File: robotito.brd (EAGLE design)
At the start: 76.2 x 76.2 mm, 53 parts, among them IC1 7805T, IC2 L298, IC3 L298, J1 22-27-2031-03, J10 22-27-2031-03, J11 22-27-2031-03, J2 22-27-2031-03, J3 22-27-2031-03, J4 22-27-2031-03, J5 22-27-2031-03, J6 22-27-2031-03, J7 22-27-2031-03, J8 22-27-2031-03, J9 22-27-2031-03

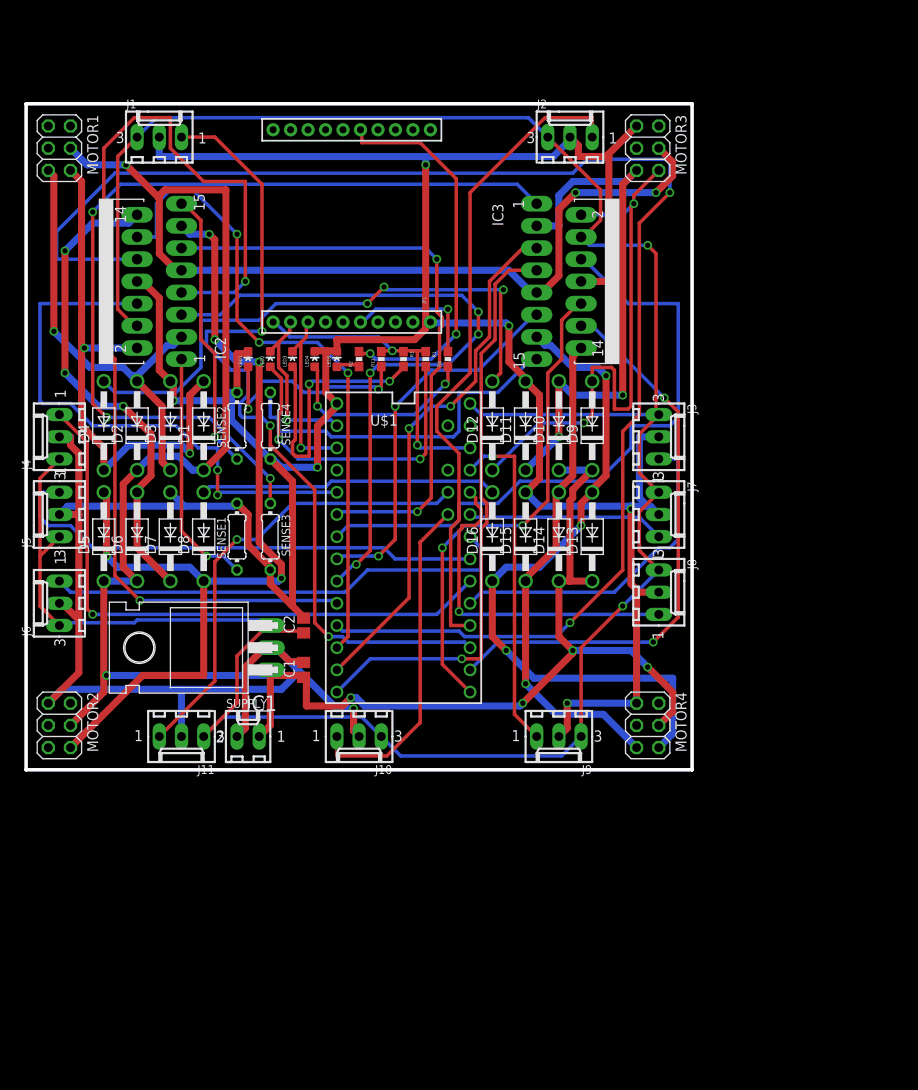
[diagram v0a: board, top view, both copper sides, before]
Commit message: Board is routing good with ~100 vias
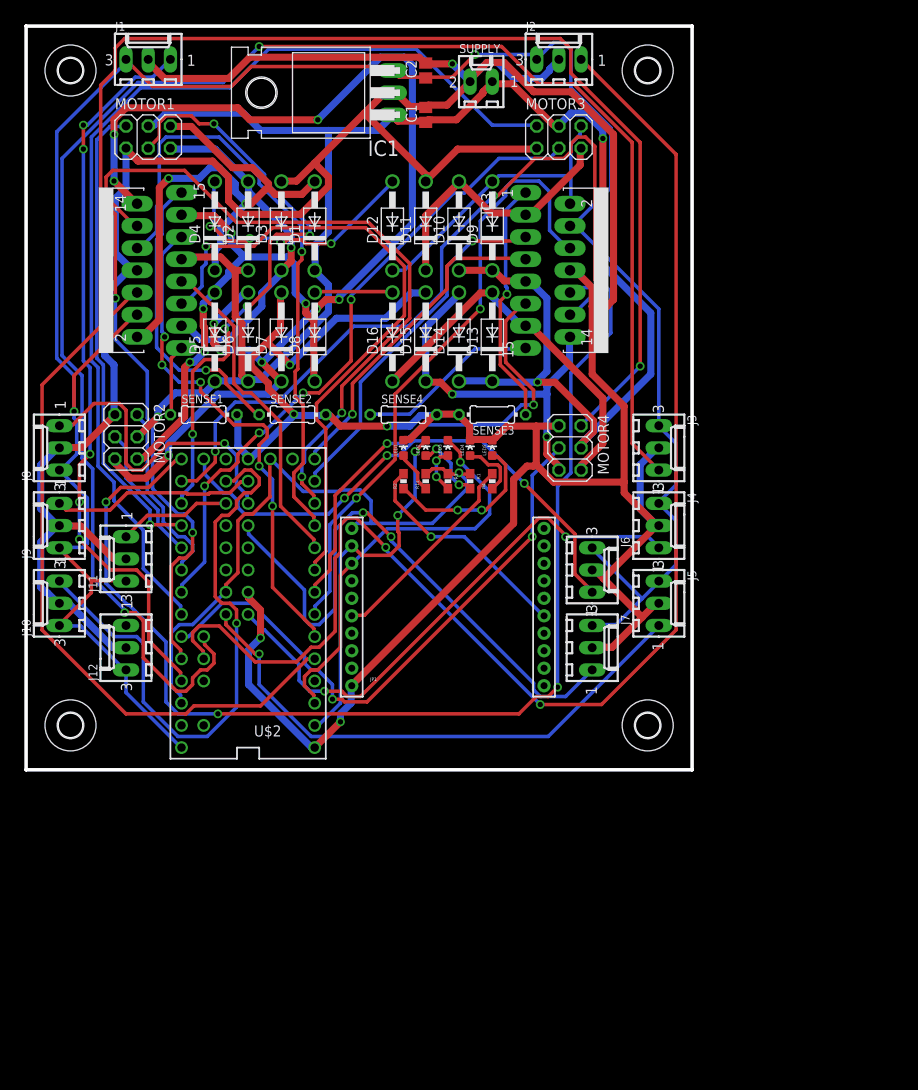
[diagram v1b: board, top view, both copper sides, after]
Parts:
- added J12: 22-27-2031-03, con-molex:6410-03
- added U$2: TEENSY_3.1-3.2_ALL_PINS&PADS, Teensy_3_and_LC_Series_Boards_v1.4:TEENSY_3.0-3.2_ALL_PINS_&_PADS
- added U$3, U$4, U$5: (no value), holes:2,8
- U$1: value TEENSY_3.1-3.2_DIL+4 -> (none); device Teensy_3_and_LC_Series_Boards_v1.4:TEENSY_3.0-3.2&LC_DIL+4 -> holes:2,8
- moved SUPPLY 79.5 mm to (52.1, 78.7)
- moved J8 70.5 mm to (3.81, 36.8), turned to 90 degrees
- moved J4 69.3 mm to (72.4, 27.9), turned to 270 degrees
- moved J5 69.3 mm to (72.4, 19.1), turned to 270 degrees
- moved U$1 66.6 mm to (5.08, 80.0)
- moved C1 65.0 mm to (45.7, 74.9)
- moved C2 65.0 mm to (45.7, 80.0)
- moved IC1 65.0 mm to (31.8, 77.5)
- moved J9 62.0 mm to (3.81, 27.9), turned to 90 degrees
- moved J6 61.1 mm to (64.8, 22.9), turned to 270 degrees
- moved JP1 54.6 mm to (48.3, 7.62), turned to 0 degrees
- moved J10 37.5 mm to (3.81, 19.1), turned to 90 degrees
- moved MOTOR2 33.9 mm to (11.4, 38.1)
- moved MOTOR4 33.0 mm to (62.2, 36.8)
- moved SENSE3 29.0 mm to (53.3, 40.6), turned to 180 degrees
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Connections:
- removed net N$33: U$1.AGND
- removed net N$34: U$1.AREF
- removed net N$36: U$1.VUSB
- removed net N$6: U$1.2
- new net AGND: U$2.AGND
- new net AREF: U$2.AREF
- new net DS12: J12.1
- new net N$15: U$2.31
- new net N$4: U$2.2
- new net VBAT: U$2.VBAT
- new net VUSB: U$2.VUSB
- net +3.3V: now also U$2.3.3V, U$2.3.3V1, U$2.3.3V2; no longer U$1.3.3V
- net +5V: now also J12.3, U$2.VIN; no longer U$1.VIN
- net DS1: now also U$2.23/A9; no longer U$1.15/A1
- net DS10: now also U$2.29; no longer U$1.A11
- net DS11: now also U$2.30; no longer U$1.A10
- net DS2: now also U$2.A10; no longer U$1.16/A2
- net DS3: now also U$2.A11; no longer U$1.17/A3
- net DS4: now also U$2.A12; no longer U$1.18/A4
- net DS5: now also U$2.A13; no longer U$1.19/A5
- net DS6: now also U$2.RESET/DAC; no longer U$1.20/A6
- net DS7: now also U$2.26; no longer U$1.21/A7
- net DS8: now also U$2.27; no longer U$1.22/A8
- net DS9: now also U$2.28; no longer U$1.23/A9
- net GND: now also J12.2, U$2.GND, U$2.GND1, U$2.GND2; no longer U$1.GND
- net M1EN: now also U$2.3; no longer U$1.3
- net M1ENCA: now also U$2.15/A1
- net M1ENCB: now also U$2.16/A2
- net M1I1: now also U$2.7; no longer U$1.7
- net M1I2: now also U$2.8; no longer U$1.8
- net M2EN: now also U$2.4; no longer U$1.4
- net M2ENCA: now also U$2.17/A3
- net M2ENCB: now also U$2.18/A4
- net M2I1: now also U$2.9; no longer U$1.9
- net M2I2: now also U$2.10; no longer U$1.10
- net M3EN: now also U$2.5; no longer U$1.5
- net M3ENCA: now also U$2.19/A5
- net M3ENCB: now also U$2.20/A6
- net M3I1: now also U$2.11; no longer U$1.11
- net M3I2: now also U$2.12; no longer U$1.12
- net M4EN: now also U$2.6; no longer U$1.6
- net M4ENCA: now also U$2.21/A7
- net M4ENCB: now also U$2.22/A8
- net M4I1: now also U$2.13; no longer U$1.13
- net M4I2: now also U$2.14/A0; no longer U$1.14/A0
- net RX: now also U$2.0; no longer U$1.0
- net TX: now also U$2.1; no longer U$1.1
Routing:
- net M4ENCB: track 0.00 -> 179.6 mm, vias 0 -> 3
- net DS3: track 38.3 -> 190.6 mm, vias 0 -> 2
- net M3ENCB: track 0.00 -> 117.7 mm
- net M2I1: track 171.6 -> 70.9 mm, vias 2 -> 1
- net DS2: track 74.5 -> 156.8 mm, vias 0 -> 2
- net M1I2: track 118.1 -> 37.9 mm, vias 2 -> 0
- net M4I1: track 56.4 -> 136.0 mm, vias 2 -> 3
- net VCC: track 296.3 -> 217.0 mm, vias 8 -> 4
- net M2M2: track 55.7 -> 134.2 mm, vias 3 -> 9
- net GND: track 431.9 -> 510.1 mm, vias 7 -> 6
- net M3ENCA: track 0.00 -> 74.7 mm, vias 0 -> 4
- net N$3: track 101.7 -> 28.1 mm, vias 3 -> 1
- net M1ENCA: track 0.00 -> 68.8 mm, vias 0 -> 5
- net M4ENCA: track 0.00 -> 67.1 mm, vias 0 -> 2
- net M1ENCB: track 0.00 -> 54.3 mm, vias 0 -> 1
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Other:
- board size 76.2 x 76.2 mm -> 76.2 x 85.1 mm

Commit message: fixed one motor connector, thinned wires
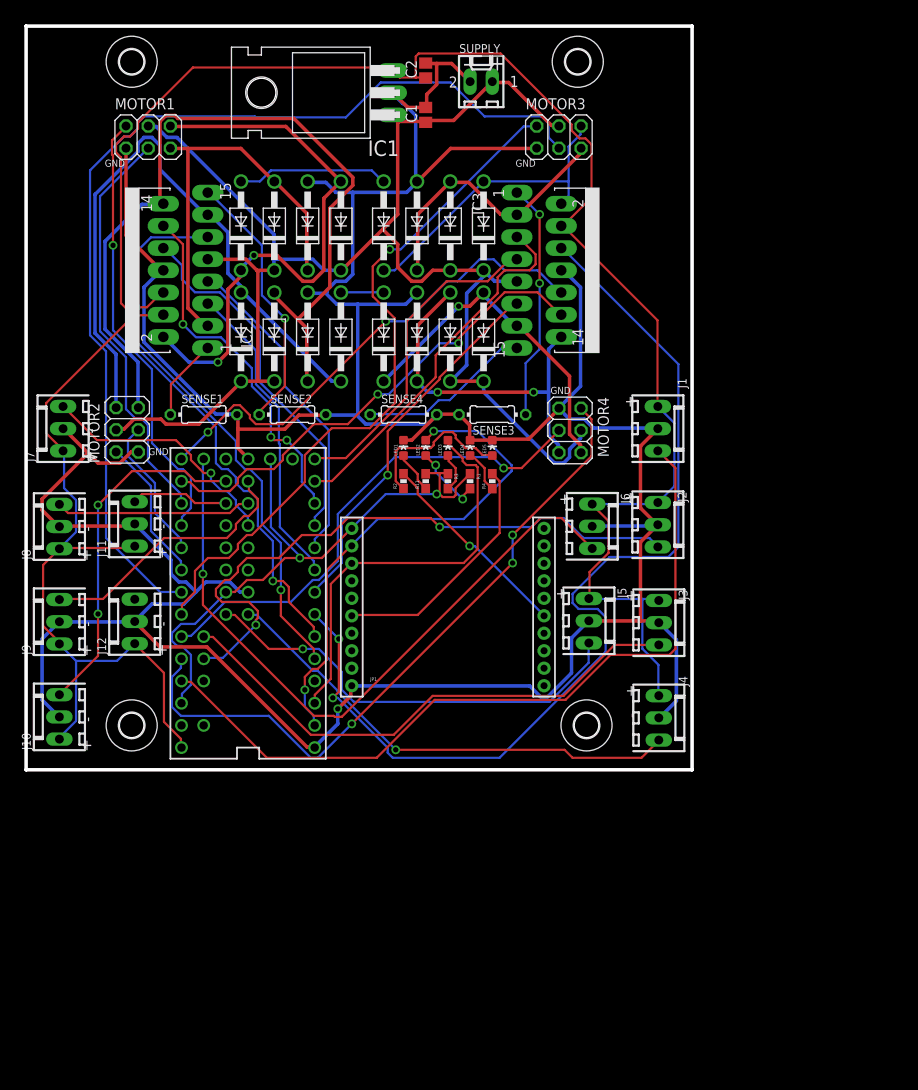
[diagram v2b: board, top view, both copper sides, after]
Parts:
- moved J1 72.0 mm to (72.3, 39.0), turned to 270 degrees
- moved J7 65.5 mm to (4.23, 39.0), turned to 90 degrees
- moved J2 54.4 mm to (72.3, 28.0), turned to 270 degrees
- moved J4 22.0 mm to (72.4, 5.94)
- moved J3 20.0 mm to (72.4, 16.8)
- moved J10 13.0 mm to (3.81, 6.05)
- moved J9 11.0 mm to (3.81, 16.9)
- moved J8 9.00 mm to (3.81, 27.8)
- moved J5 8.25 mm to (64.4, 17.1)
- moved U$3 8.06 mm to (63.1, 81.0)
- moved U$1 7.07 mm to (12.1, 81.0)
- moved U$4 7.00 mm to (64.1, 5.08)
- moved U$5 7.00 mm to (12.1, 5.08)
- moved J6 5.00 mm to (64.8, 27.9)
- moved J11 4.12 mm to (12.4, 28.1)
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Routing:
- net DS3: track 190.6 -> 61.0 mm, vias 2 -> 0
- net M4ENCB: track 179.6 -> 78.5 mm
- net GND: track 510.1 -> 419.1 mm, vias 6 -> 1
- net DS2: track 156.8 -> 72.1 mm
- net M4I1: track 136.0 -> 56.7 mm, vias 3 -> 2
- net VCC: track 217.0 -> 174.0 mm, vias 4 -> 0
- net M3EN: track 71.3 -> 114.1 mm
- net M3ENCA: track 74.7 -> 116.4 mm, vias 4 -> 0
- net M2M2: track 134.2 -> 94.5 mm, vias 9 -> 0
- net DS7: track 67.8 -> 28.5 mm, vias 2 -> 1
- net M2I2: track 79.9 -> 41.6 mm, vias 2 -> 3
- net M1I1: track 73.3 -> 35.7 mm, vias 1 -> 0
- net M3ENCB: track 117.7 -> 80.7 mm, vias 0 -> 1
- net M4I2: track 92.4 -> 55.5 mm, vias 3 -> 2
- net M2I1: track 70.9 -> 41.7 mm, vias 1 -> 0
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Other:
- board text added: "+"
- board text added: "-"
- board text added: "GND"

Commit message: fixed some errors/warnings
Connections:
- removed net CTS: JP1.12
- removed net DIO0: JP1.20
- removed net DIO1: JP1.19
- removed net DIO11: JP1.7
- removed net DIO12: JP1.4
- removed net DIO2: JP1.18
- removed net DIO3: JP1.17
- removed net DIO4: JP1.11
- removed net DIO9: JP1.13
- removed net DTR: JP1.9
- removed net N$1: D12.A, D4.A
- removed net N$15: U$2.31
- removed net N$2: D16.A, D8.A
- removed net N$4: U$2.2
- removed net RES: JP1.8
- removed net RES2: JP1.14
- removed net RESET: JP1.5
- removed net RTS: JP1.16
- net DS12: now also U$2.31
- net GND: now also D12.A, D16.A, D4.A, D8.A
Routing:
- net GND: track 419.1 -> 444.1 mm
- net N$1: track 17.4 -> 0.00 mm
- net DS12: track 0.00 -> 14.5 mm, vias 0 -> 1
- net N$2: track 4.90 -> 0.00 mm
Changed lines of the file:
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@@
 <?xml version="1.0" encoding="utf-8"?>
 <!DOCTYPE eagle SYSTEM "eagle.dtd">
-<eagle version="7.7.0">
+<eagle version="7.6.0">
 <drawing>
 <settings>
@@
 <wire x1="34.4043" y1="54.864" x2="34.4043" y2="54.6354" width="0.4064" layer="16"/>
 <wire x1="35.433" y1="55.8927" x2="34.4043" y2="54.864" width="0.4064" layer="16"/>
-<wire x1="36.576" y1="55.8927" x2="35.433" y2="55.8927" width="0.4064" layer="16"/>
+<wire x1="36.576" y1="55.8927" x2="36" y2="55.8927" width="0.4064" layer="16"/>
+<wire x1="36" y1="55.8927" x2="35.433" y2="55.8927" width="0.4064" layer="16"/>
 <wire x1="37.3761" y1="56.6928" x2="36.576" y2="55.8927" width="0.4064" layer="16"/>
 <wire x1="37.3761" y1="66.0654" x2="37.3761" y2="56.6928" width="0.4064" layer="16"/>
@@
 <wire x1="64.3509" y1="17.0307" x2="64.39" y2="17.05" width="0.4064" layer="16"/>
 <via x="35.6616" y="6.9723" extent="1-16" drill="0.6096"/>
+<contactref element="D8" pad="A"/>
+<contactref element="D16" pad="A"/>
+<wire x1="40.8051" y1="54.6354" x2="36.1188" y2="54.6354" width="0.254" layer="16"/>
+<wire x1="36.1188" y1="54.6354" x2="36.02" y2="54.61" width="0.254" layer="16"/>
+<wire x1="40.8051" y1="54.6354" x2="40.91" y2="54.61" width="0.254" layer="16"/>
+<contactref element="D12" pad="A"/>
+<contactref element="D4" pad="A"/>
+<wire x1="26.7462" y1="67.3227" x2="24.6888" y2="67.3227" width="0.254" layer="16"/>
+<wire x1="28.0035" y1="68.58" x2="26.7462" y2="67.3227" width="0.254" layer="16"/>
+<wire x1="39.5478" y1="68.58" x2="32.25" y2="68.58" width="0.254" layer="16"/>
+<wire x1="32.25" y1="68.58" x2="28.0035" y2="68.58" width="0.254" layer="16"/>
+<wire x1="40.8051" y1="67.3227" x2="40.6889" y2="67.4389" width="0.254" layer="16"/>
+<wire x1="40.6889" y1="67.4389" x2="39.5478" y2="68.58" width="0.254" layer="16"/>
+<wire x1="24.6888" y1="67.3227" x2="24.59" y2="67.31" width="0.254" layer="16"/>
+<wire x1="40.75" y1="67.5" x2="40.91" y2="67.31" width="0.4064" layer="16"/>
+<wire x1="40.75" y1="67.5" x2="40.6889" y2="67.4389" width="0.4064" layer="16"/>
+<wire x1="32.25" y1="67.5" x2="32.25" y2="68.58" width="0.4064" layer="16"/>
+<wire x1="32.25" y1="67.5" x2="32.21" y2="67.31" width="0.4064" layer="16"/>
+<wire x1="36" y1="55.8927" x2="36" y2="54.75" width="0.4064" layer="16"/>
+<wire x1="36" y1="54.75" x2="36.02" y2="54.61" width="0.4064" layer="16"/>
 </signal>
 <signal name="M1ENCB">
@@
 <via x="29.6037" y="51.6636" extent="1-16" drill="0.6096"/>
 </signal>
-<signal name="N$1">
-<contactref element="D4" pad="A"/>
-<contactref element="D12" pad="A"/>
-<wire x1="26.7462" y1="67.3227" x2="24.6888" y2="67.3227" width="0.254" layer="16"/>
-<wire x1="28.0035" y1="68.58" x2="26.7462" y2="67.3227" width="0.254" layer="16"/>
-<wire x1="39.5478" y1="68.58" x2="28.0035" y2="68.58" width="0.254" layer="16"/>
-<wire x1="40.8051" y1="67.3227" x2="39.5478" y2="68.58" width="0.254" layer="16"/>
-<wire x1="24.6888" y1="67.3227" x2="24.59" y2="67.31" width="0.254" layer="16"/>
-<wire x1="40.8051" y1="67.3227" x2="40.91" y2="67.31" width="0.254" layer="16"/>
-</signal>
-<signal name="N$2">
-<contactref element="D8" pad="A"/>
-<contactref element="D16" pad="A"/>
-<wire x1="40.8051" y1="54.6354" x2="36.1188" y2="54.6354" width="0.254" layer="16"/>
-<wire x1="36.1188" y1="54.6354" x2="36.02" y2="54.61" width="0.254" layer="16"/>
-<wire x1="40.8051" y1="54.6354" x2="40.91" y2="54.61" width="0.254" layer="16"/>
-</signal>
 <signal name="N$3">
 <contactref element="IC3" pad="1"/>
@@
 <via x="46.9773" y="31.5468" extent="1-16" drill="0.6096"/>
 </signal>
-<signal name="DIO4">
-<contactref element="JP1" pad="11"/>
-</signal>
-<signal name="CTS">
-<contactref element="JP1" pad="12"/>
-</signal>
-<signal name="DIO9">
-<contactref element="JP1" pad="13"/>
-</signal>
-<signal name="RES2">
-<contactref element="JP1" pad="14"/>
-</signal>
-<signal name="RTS">
-<contactref element="JP1" pad="16"/>
-</signal>
-<signal name="DIO3">
-<contactref element="JP1" pad="17"/>
-</signal>
-<signal name="DIO2">
-<contactref element="JP1" pad="18"/>
-</signal>
-<signal name="DIO1">
-<contactref element="JP1" pad="19"/>
-</signal>
-<signal name="DIO0">
-<contactref element="JP1" pad="20"/>
-</signal>
-<signal name="DTR">
-<contactref element="JP1" pad="9"/>
-</signal>
-<signal name="RES">
-<contactref element="JP1" pad="8"/>
-</signal>
-<signal name="DIO11">
-<contactref element="JP1" pad="7"/>
-</signal>
-<signal name="DIO12">
-<contactref element="JP1" pad="4"/>
-</signal>
-<signal name="RESET">
-<contactref element="JP1" pad="5"/>
-</signal>
 <signal name="DIO5">
 <contactref element="JP1" pad="15"/>
@@
 <contactref element="U$2" pad="VUSB"/>
 </signal>
-<signal name="N$4">
-<contactref element="U$2" pad="2"/>
-</signal>
-<signal name="N$15">
-<contactref element="U$2" pad="31"/>
-</signal>
 <signal name="DS12">
 <contactref element="J12" pad="1"/>
+<contactref element="U$2" pad="31"/>
+<wire x1="21.25" y1="26.25" x2="22.75" y2="27.75" width="0.254" layer="16"/>
+<wire x1="21.25" y1="25.5" x2="21.25" y2="26.25" width="0.254" layer="16"/>
+<wire x1="19.5" y1="25.5" x2="21.25" y2="25.5" width="0.254" layer="1"/>
+<wire x1="18" y1="24" x2="19.5" y2="25.5" width="0.254" layer="1"/>
+<wire x1="16.75" y1="24" x2="18" y2="24" width="0.254" layer="1"/>
+<wire x1="12.5" y1="19.75" x2="16.75" y2="24" width="0.254" layer="1"/>
+<wire x1="22.75" y1="27.75" x2="22.86" y2="27.94" width="0.254" layer="16"/>
+<wire x1="12.5" y1="19.75" x2="12.43" y2="19.51" width="0.254" layer="1"/>
+<via x="21.25" y="25.5" extent="1-16" drill="0.6096"/>
 </signal>
 <signal name="AREF">

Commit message: juan and tj improvements draft
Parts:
- removed J1, J10, J11, J12, J2, J3, J4, J5, J6, J7, J8, J9: 22-27-2031-03, con-molex:6410-03
- removed SENSE1, SENSE2, SENSE3, SENSE4: .5, resistor:0204/7
- added JP2, JP3: (no value), pinhead:2X06
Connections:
- removed net N$10: IC2.1, SENSE1.1
- removed net N$11: IC2.15, SENSE2.1
- removed net N$3: IC3.1, SENSE3.1
- removed net N$8: IC3.15, SENSE4.1
- new net HB1GND: IC2.8
- new net HB2GND: IC3.8
- net +5V: now also IC2.9, IC3.9; no longer IC2.4, IC3.4, J1.3, J10.3, J11.3, J12.3, J2.3, J3.3, J4.3, J5.3, J6.3, J7.3, J8.3, J9.3
- net DS1: no longer J1.1
- net DS10: no longer J10.1
- net DS11: no longer J11.1
- net DS12: no longer J12.1
- net DS2: no longer J2.1
- net DS3: no longer J3.1
- net DS4: no longer J4.1
- net DS5: no longer J5.1
- net DS6: no longer J6.1
- net DS7: no longer J7.1
- net DS8: no longer J8.1
- net DS9: no longer J9.1
- net GND: now also IC2.1, IC2.15, IC3.1, IC3.15; no longer IC2.8, IC3.8, J1.2, J10.2, J11.2, J12.2, J2.2, J3.2, J4.2, J5.2, J6.2, J7.2, J8.2, J9.2, SENSE1.2, SENSE2.2, SENSE3.2, SENSE4.2
- net VCC: now also IC2.4, IC3.4; no longer IC2.9, IC3.9
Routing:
- net GND: track 444.1 -> 323.3 mm, vias 1 -> 2
- net +5V: track 268.5 -> 183.1 mm, vias 0 -> 2
- net DS1: track 88.9 -> 170.3 mm
- net M4I1: track 56.7 -> 126.1 mm, vias 2 -> 3
- net M2M2: track 94.5 -> 59.8 mm, vias 0 -> 3
- net VCC: track 174.0 -> 204.9 mm, vias 0 -> 2
- net N$11: track 30.4 -> 0.00 mm, vias 1 -> 0
- net M3ENCB: track 80.7 -> 109.9 mm, vias 1 -> 3
- net N$3: track 27.2 -> 0.00 mm, vias 2 -> 0
- net M4ENCA: track 57.2 -> 83.3 mm, vias 1 -> 4
- net M2M1: track 73.1 -> 47.2 mm
- net M4EN: track 42.9 -> 67.5 mm, vias 1 -> 3
- net M2EN: track 63.6 -> 87.3 mm, vias 1 -> 6
- net M3EN: track 114.1 -> 91.0 mm, vias 2 -> 4
- net M2I2: track 41.6 -> 63.1 mm, vias 3 -> 2
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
